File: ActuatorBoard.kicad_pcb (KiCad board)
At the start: 2 copper layers, 75 x 89.5 mm, 79 parts, among them J1 Screw_Terminal_01x02, J11 Screw_Terminal_01x02, J12 Screw_Terminal_01x02, J13 Screw_Terminal_01x04, J2 Screw_Terminal_01x02, J3 Screw_Terminal_01x02, J4 Screw_Terminal_01x02, J5 Screw_Terminal_01x02, J7 Screw_Terminal_01x02, J8 Screw_Terminal_01x02, J9 Screw_Terminal_01x02, K1 SANYOU_SRD_Form_B, K2 SANYOU_SRD_Form_B, K3 SANYOU_SRD_Form_B, P1 CONN_01X03, P10 CONN_01X03, P11 CONN_01X03, P12 CONN_01X03, P13 CONN_01X02, P14 SERVO_+, P15 SERVO_-, P16 CONN_01X03, P17 CONN_01X05, P18 CONN_01X08, P19 CONN_01X05, P2 CAN_Conn, P20 CONN_01X08, P21 STEPPER_VCC, P22 CONN_01X05, P23 CONN_01X04, P3 CONN_01X03, P4 CONN_01X03, P5 CONN_01X03, P7 CONN_01X03, P8 CONN_01X03, Q1 BS170, Q2 BS170, Q3 BS170, Q5 IRLR024, U1 MCP2551-I-SN, U2 AT90CAN128-16AU, U3 ULN2003, U4 L7805, Y1 Crystal, Y2 Crystal

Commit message: Added output files
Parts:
- added P6: CONN_01X06, Pin_Headers:Pin_Header_Straight_1x06, F.Cu at (181.4, 76.3)
- added REF**: 1pin, Connect:1pin, F.Cu at (199.1, 105.4)
- added REF**: 1pin, Connect:1pin, F.Cu at (202.3, 79.6)
- added REF**: 1pin, Connect:1pin, F.Cu at (220.3, 65.6)
- added REF**: 1pin, Connect:1pin, F.Cu at (208.5, 43.0)
- added REF**: 1pin, Connect:1pin, F.Cu at (176.1, 49.4)
- moved P20 22.5 mm to (167.1, 26.2), turned to 90 degrees
- moved P18 22.2 mm to (167.1, 28.8), turned to 90 degrees
- moved J3 20.9 mm to (233.2, 29.4), turned to 180 degrees
- moved D3 16.3 mm to (200.2, 43.6)
- moved R9 14.5 mm to (200.2, 41.7), turned to 0 degrees
- moved D7 11.6 mm to (227.9, 46.9), turned to 180 degrees
- moved R10 10.1 mm to (224.3, 46.9), turned to 0 degrees
- moved J2 9.71 mm to (222.5, 29.4), turned to 180 degrees
- moved C4 9.59 mm to (208.4, 36.7), turned to 0 degrees
- moved C2 9.00 mm to (209.6, 36.7), turned to 180 degrees
- moved D2 7.89 mm to (212.3, 28.5), turned to 90 degrees
- moved C3 5.47 mm to (219.7, 42.9), turned to 270 degrees
- moved D8 5.15 mm to (234.9, 97.2), turned to 180 degrees
- moved Q5 4.27 mm to (234.3, 41.4)
- moved D10 3.90 mm to (163.1, 94.2), turned to 0 degrees
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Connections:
- P22 pad 1: +5V -> PF2
- P22 pad 2: +5V -> PF2
- P22 pad 3: +5V -> PF2
- P22 pad 4: +5V -> PF2
- P22 pad 5: +5V -> PF2
- R11 pad 2: Net-(R11-Pad2) -> D2
- R12 pad 2: Net-(R12-Pad2) -> D1
- S1 pad 3: RX0 -> TX0
- S1 pad 4: TX0 -> RX0
- U2 pad 10: STEP -> DIRECTION
- U2 pad 11: DIRECTION -> STEP
- U2 pad 20: (no net) -> RESET
- U2 pad 44: Net-(R11-Pad2) -> MINI_M3
- U2 pad 45: Net-(R12-Pad2) -> MINI_M2
- U2 pad 46: MINI_M3 -> D2
- U2 pad 47: MINI_M2 -> D1
- U3 pad 1: R1 -> R2
- U3 pad 13: R2_SIG -> R1_SIG
- U3 pad 14: R2_SIG -> R1_SIG
- U3 pad 15: R1_SIG -> R2_SIG
- U3 pad 16: R1_SIG -> R2_SIG
- U3 pad 2: R1 -> R2
- U3 pad 3: R2 -> R1
- U3 pad 4: R2 -> R1
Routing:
- net PF2: track 0.00 -> 292.9 mm, vias 0 -> 2
- net +12V: track 0.00 -> 226.9 mm, vias 0 -> 4
- net +5V: track 0.00 -> 158.3 mm, vias 0 -> 5
- net GND: track 0.00 -> 121.1 mm, vias 0 -> 5
- net PC7: track 0.00 -> 58.2 mm, vias 0 -> 2
- net PC6: track 0.00 -> 52.8 mm, vias 0 -> 2
- net PC5: track 0.00 -> 49.8 mm, vias 0 -> 2
- net TX0: track 0.00 -> 43.9 mm, vias 0 -> 3
- net RX0: track 0.00 -> 41.6 mm, vias 0 -> 4
- net PC4: track 0.00 -> 41.4 mm
- net PC3: track 0.00 -> 38.7 mm
- net MINI_M3: track 0.00 -> 37.8 mm, vias 0 -> 2
- net PC2: track 0.00 -> 36.8 mm
- net STEP: track 0.00 -> 36.6 mm, vias 0 -> 1
- net PC1: track 0.00 -> 34.9 mm
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- added copper zone on B.Cu, net GND
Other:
- board text added: "3"
- board text added: "3A"
- board text added: "3B"
- board text added: "3C"
- board text added: "4"
- board text added: "5"
- board text added: "5VD"
- board text added: "6"
- board text added: "7"
- board text added: "AX-12"
- board text added: "F0"
- board text added: "F1"
- board text added: "GND"
- board text added: "H"
- board text added: "L"
- board text added: "ON=AX|OFF=PROG"
- board text added: "PB"
- board text added: "PC0"
- board text added: "PC1"
- board text added: "PC2"
- board text added: "PC3"
- board text added: "PC4"
- board text added: "PC5"
- board text added: "PC7"
- board text added: "RE"
- board text added: "RX"
- board text added: "SCK"
- board text added: "SCL"
- board text added: "SDA"
- board text added: "TX"
- board text added: "VCC"
- board text added: "http://elektropioneer.co.rs/ https://github.com/Elektropioneer Actuator Board V1"

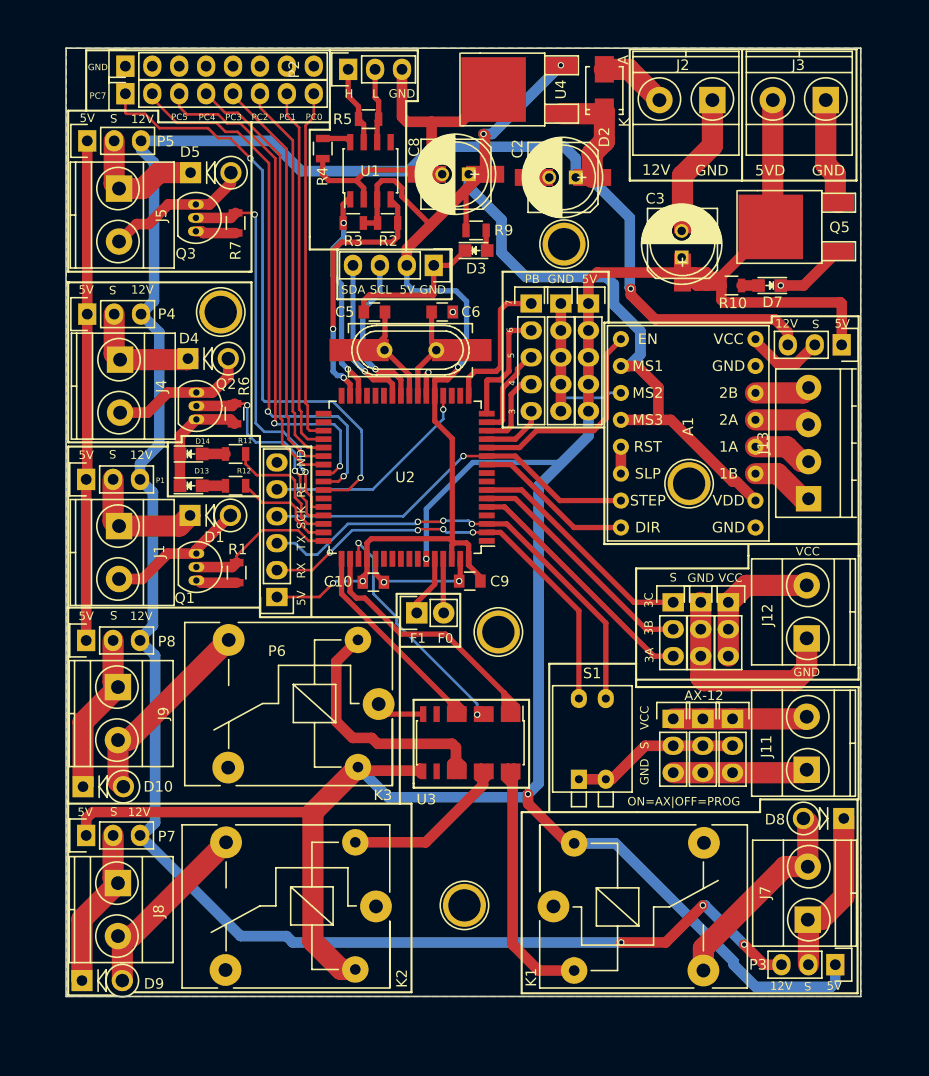
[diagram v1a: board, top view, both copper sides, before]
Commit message: Added new pdf, added tx rx debug pins
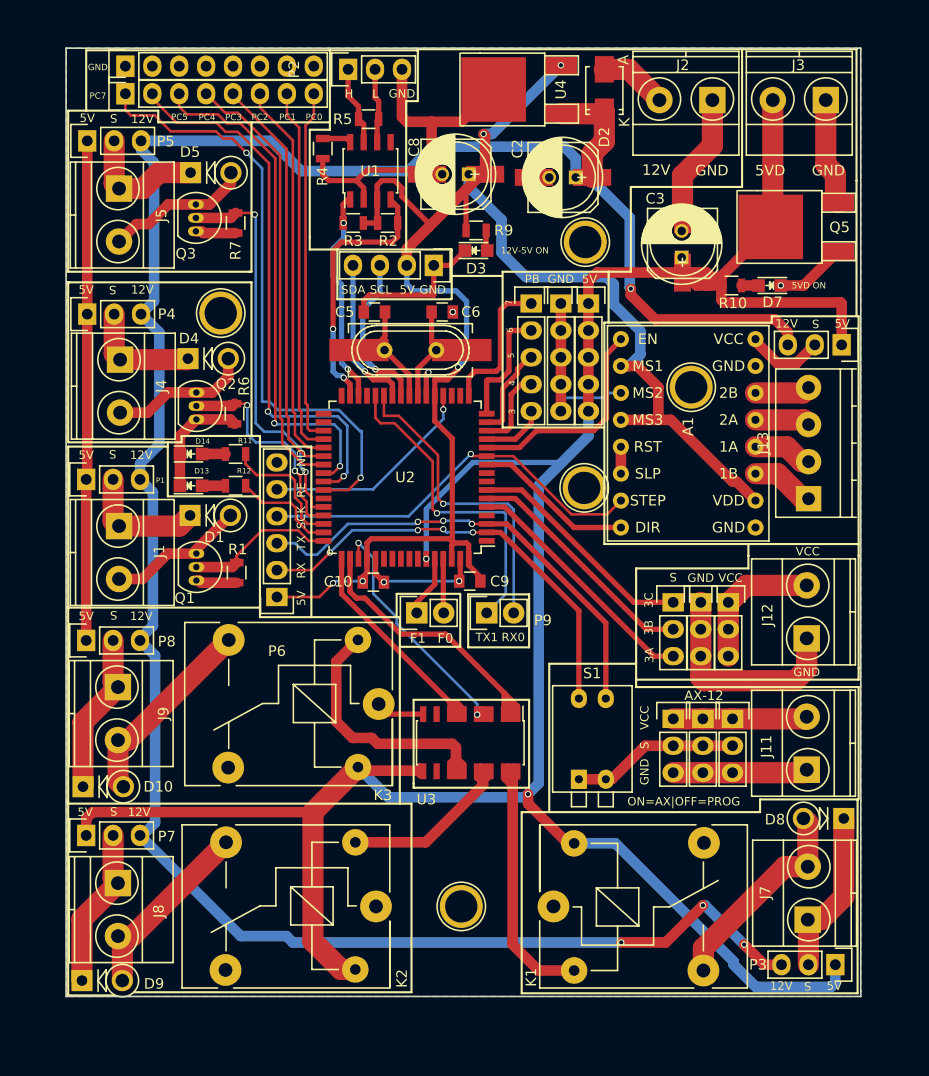
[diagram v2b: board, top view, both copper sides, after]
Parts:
- removed the REF** at (199.1, 105.4)
- removed the REF** at (202.3, 79.6)
- removed the REF** at (220.3, 65.6)
- removed the REF** at (208.5, 43.0)
- removed the REF** at (176.1, 49.4)
- added P9: CONN_01X02, Pin_Headers:Pin_Header_Straight_1x02, F.Cu at (201.2, 77.8)
- added REF**: 1pin, Connect:1pin, F.Cu at (176.1, 49.5)
- added REF**: 1pin, Connect:1pin, F.Cu at (210.5, 42.8)
- added REF**: 1pin, Connect:1pin, F.Cu at (220.5, 56.5)
- added REF**: 1pin, Connect:1pin, F.Cu at (198.8, 105.5)
- added REF**: 1pin, Connect:1pin, F.Cu at (210.4, 66.0)
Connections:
- U2 pad 27: (no net) -> RX1
- U2 pad 28: (no net) -> TX1
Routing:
- net TX1: track 0.00 -> 31.1 mm, vias 0 -> 1
- net RX1: track 0.00 -> 30.0 mm, vias 0 -> 1
- net STEP: track 36.6 -> 37.8 mm
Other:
- board text added: "12V-5V ON"
- board text added: "5VD ON"
- board text added: "RX0"
- board text added: "TX1"

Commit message: Added new wrl files, and did repairs
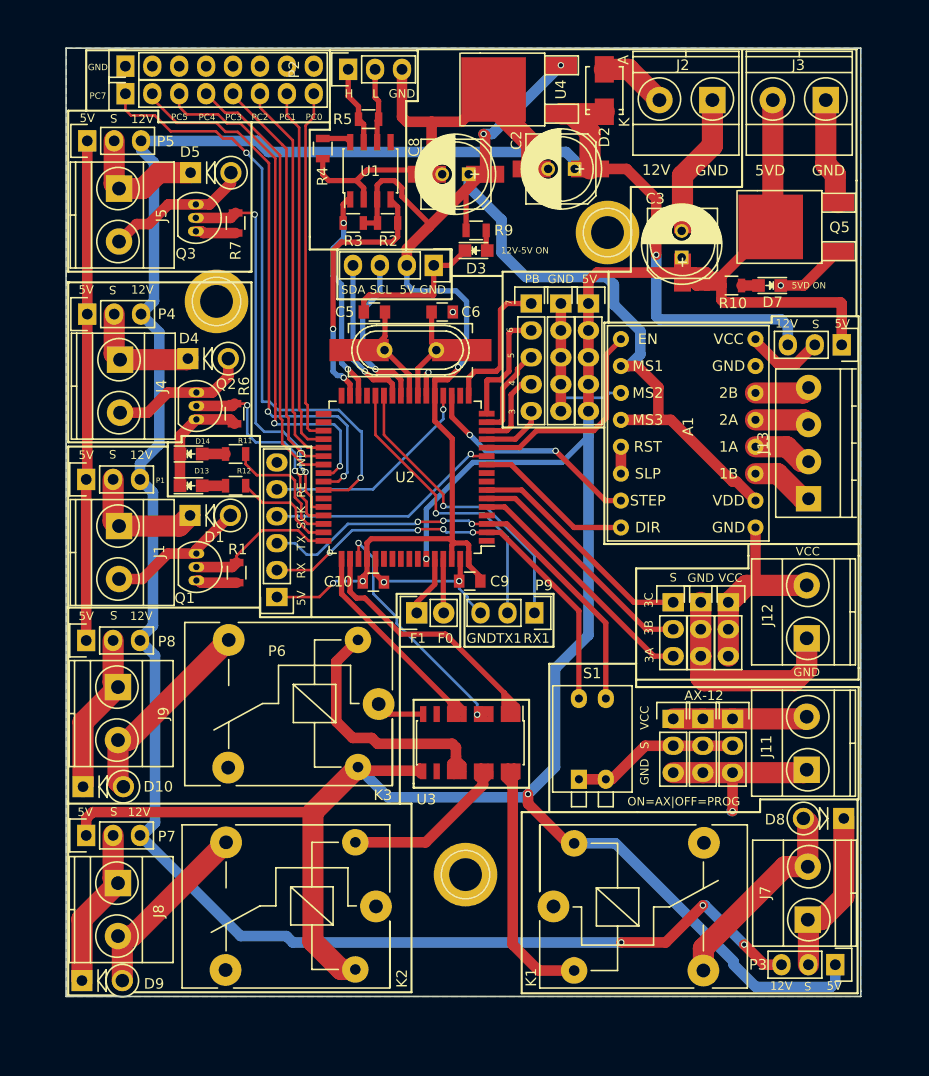
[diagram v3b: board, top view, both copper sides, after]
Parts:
- removed the REF** at (176.1, 49.5)
- removed the REF** at (210.5, 42.8)
- removed the REF** at (220.5, 56.5)
- removed the REF** at (198.8, 105.5)
- removed the REF** at (210.4, 66.0)
- added REF**: 1pin, Connect:1pin, F.Cu at (175.7, 48.4)
- added REF**: 1pin, Connect:1pin, F.Cu at (199.2, 102.5)
- added REF**: 1pin, Connect:1pin, F.Cu at (212.6, 41.9)
- C1, C2, C3, C4, C7, C8: value CP -> 100u
- C10, C9: value C -> 100n
- P9: value CONN_01X02 -> CONN_01X03; footprint Pin_Headers:Pin_Header_Straight_1x02 -> Pin_Headers:Pin_Header_Straight_1x03
- R10, R11, R12, R9: value 1K -> 330
- moved P9 4.50 mm to (205.7, 77.8), turned to 270 degrees
- moved C4 0.82 mm to (208.2, 35.9)
- moved C2 0.81 mm to (209.5, 35.9)
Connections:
- J11 pad 1: Net-(J11-Pad1) -> GND
- J12 pad 2: Net-(J12-Pad2) -> GND
- P10 pad 3: Net-(J11-Pad1) -> GND
- P11 pad 3: Net-(J11-Pad1) -> GND
- P12 pad 3: Net-(J11-Pad1) -> GND
- P15 pad 1: Net-(J12-Pad2) -> GND
- P15 pad 2: Net-(J12-Pad2) -> GND
- P15 pad 3: Net-(J12-Pad2) -> GND
- P6 pad 4: STEP -> SCK
- P9 pad 1: TX1 -> RX1
- P9 pad 2: RX1 -> TX1
- U2 pad 11: STEP -> SCK
- U2 pad 19: (no net) -> STEP
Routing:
- net GND: track 121.1 -> 169.2 mm, vias 5 -> 6
- net SCK: track 0.00 -> 22.3 mm, vias 0 -> 1
- net STEP: track 37.8 -> 21.2 mm, vias 1 -> 2
- net Net-(J12-Pad2): track 13.1 -> 0.00 mm
- net Net-(J11-Pad1): track 12.7 -> 0.00 mm
- net TX1: track 31.1 -> 28.4 mm
- net RX1: track 30.0 -> 28.7 mm
- net +12V: track 226.9 -> 225.9 mm
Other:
- board text added: "RX1"
- board text removed: "RX0"

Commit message: 12V relays...
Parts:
- removed REF** (x3): 1pin, Connect:1pin
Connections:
- K1 pad 5: PF2 -> +12V
- K2 pad 5: PF2 -> +12V
- K3 pad 5: PF2 -> +12V
- U3 pad 9: PF2 -> +12V
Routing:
- net +12V: track 225.9 -> 272.4 mm
- net GND: track 169.2 -> 206.1 mm, vias 6 -> 8
- net PF2: track 293.3 -> 306.0 mm, vias 2 -> 3

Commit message: 12V...
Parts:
- added REF**: 1pin, Connect:1pin, F.Cu at (175.7, 48.5)
- added REF**: 1pin, Connect:1pin, F.Cu at (199.1, 105.2)
- added REF**: 1pin, Connect:1pin, F.Cu at (212.6, 41.8)
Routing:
- net GND: track 206.1 -> 231.0 mm, vias 8 -> 12
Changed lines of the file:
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@@
     (area 161.424999 24.424999 236.575001 114.075001)
     (thickness 1.6)
-    (drawings 206)
-    (tracks 903)
+    (drawings 205)
+    (tracks 912)
     (zones 0)
-    (modules 81)
+    (modules 84)
     (nets 79)
   )
@@
     )
   )
-  (dimension 3.1 (width 0.3) (layer Dwgs.User)
-    (gr_text "3,100 mm" (at 155.35 48.35 270) (layer Dwgs.User)
-      (effects (font (size 1.5 1.5) (thickness 0.3)))
+  (module Connect:1pin (layer F.Cu)
+    (at 175.7 48.5)
+    (descr "module 1 pin (ou trou mecanique de percage)")
+    (tags DEV)
+    (fp_text reference REF** (at 0 -3.048) (layer F.SilkS) hide
+      (effects (font (size 1 1) (thickness 0.15)))
+    )
+    (fp_text value 1pin (at 0 2.794) (layer F.Fab) hide
+      (effects (font (size 1 1) (thickness 0.15)))
+    )
+    (fp_circle (center 0 0) (end 0 -2.286) (layer F.SilkS) (width 0.15))
+    (pad 1 thru_hole circle (at 0 0) (size 6 6) (drill 3.1) (layers *.Cu *.Mask F.SilkS))
+  )
+  (module Connect:1pin (layer F.Cu)
+    (at 199.1 105.2)
+    (descr "module 1 pin (ou trou mecanique de percage)")
+    (tags DEV)
+    (fp_text reference REF** (at 0 -3.048) (layer F.SilkS) hide
+      (effects (font (size 1 1) (thickness 0.15)))
+    )
+    (fp_text value 1pin (at 0 2.794) (layer F.Fab) hide
+      (effects (font (size 1 1) (thickness 0.15)))
+    )
+    (fp_circle (center 0 0) (end 0 -2.286) (layer F.SilkS) (width 0.15))
+    (pad 1 thru_hole circle (at 0 0) (size 6 6) (drill 3.1) (layers *.Cu *.Mask F.SilkS))
+  )
+  (module Connect:1pin (layer F.Cu)
+    (at 212.6 41.8)
+    (descr "module 1 pin (ou trou mecanique de percage)")
+    (tags DEV)
+    (fp_text reference REF** (at 0 -3.048) (layer F.SilkS) hide
+      (effects (font (size 1 1) (thickness 0.15)))
+    )
+    (fp_text value 1pin (at 0 2.794) (layer F.Fab) hide
+      (effects (font (size 1 1) (thickness 0.15)))
     )
-    (feature1 (pts (xy 175.7 49.95) (xy 156.8 49.95)))
-    (feature2 (pts (xy 175.7 46.85) (xy 156.8 46.85)))
-    (crossbar (pts (xy 159.5 46.85) (xy 159.5 49.95)))
-    (arrow1a (pts (xy 159.5 49.95) (xy 158.913579 48.823496)))
-    (arrow1b (pts (xy 159.5 49.95) (xy 160.086421 48.823496)))
-    (arrow2a (pts (xy 159.5 46.85) (xy 158.913579 47.976504)))
-    (arrow2b (pts (xy 159.5 46.85) (xy 160.086421 47.976504)))
+    (fp_circle (center 0 0) (end 0 -2.286) (layer F.SilkS) (width 0.15))
+    (pad 1 thru_hole circle (at 0 0) (size 6 6) (drill 3.1) (layers *.Cu *.Mask F.SilkS))
   )
   (gr_text RX1 (at 205.9 80.2) (layer F.SilkS)
@@
     (effects (font (size 0.8 0.8) (thickness 0.2)))
   )
-  (segment (start 211.85 89.65) (end 211.9 89.65) (width 1) (layer B.Cu) (net 1))
-  (via (at 204.65 83.85) (size 0.6) (drill 0.4) (layers F.Cu B.Cu) (net 1))
-  (segment (start 204.65 84.2) (end 204.65 83.85) (width 1) (layer F.Cu) (net 1))
-  (segment (start 209.25 88.8) (end 204.65 84.2) (width 1) (layer F.Cu) (net 1))
-  (segment (start 211.05 88.8) (end 209.25 88.8) (width 1) (layer F.Cu) (net 1))
-  (segment (start 211.9 89.65) (end 211.05 88.8) (width 1) (layer F.Cu) (net 1))
-  (via (at 211.9 89.65) (size 0.6) (drill 0.4) (layers F.Cu B.Cu) (net 1))
-  (segment (start 181.4 63.6) (end 181.4 63.25) (width 1) (layer F.Cu) (net 1) (status C00000))
-  (segment (start 181.4 63.25) (end 180.25 62.1) (width 1) (layer F.Cu) (net 1) (status 400000))
+  (via (at 220.1 53) (size 0.6) (drill 0.4) (layers F.Cu B.Cu) (net 1))
+  (via (at 221.6 48.1) (size 0.6) (drill 0.4) (layers F.Cu B.Cu) (net 1))
+  (segment (start 221.6 48.1) (end 221.6 51.5) (width 1) (layer F.Cu) (net 1))
+  (segment (start 221.6 51.5) (end 220.1 53) (width 1) (layer F.Cu) (net 1))
+  (segment (start 204.6 84.3) (end 204.7 84.3) (width 1) (layer B.Cu) (net 1))
+  (via (at 210.6 88.5) (size 0.6) (drill 0.4) (layers F.Cu B.Cu) (net 1))
+  (segment (start 208.9 88.5) (end 210.6 88.5) (width 1) (layer F.Cu) (net 1))
+  (segment (start 204.7 84.3) (end 208.9 88.5) (width 1) (layer F.Cu) (net 1))
+  (via (at 204.7 84.3) (size 0.6) (drill 0.4) (layers F.Cu B.Cu) (net 1))
+  (segment (start 207.5 105.5) (end 207.5 102.3) (width 1) (layer F.Cu) (net 1) (status 400000))
+  (via (at 205.2 95.1) (size 0.6) (drill 0.4) (layers F.Cu B.Cu) (net 1))
+  (segment (start 205.2 100) (end 205.2 95.1) (width 1) (layer F.Cu) (net 1))
+  (segment (start 207.5 102.3) (end 205.2 100) (width 1) (layer F.Cu) (net 1))
+  (segment (start 190.75 105.5) (end 191.9 105.5) (width 1) (layer F.Cu) (net 1) (status C00000))
+  (segment (start 191.9 105.5) (end 198.3 99.1) (width 1) (layer F.Cu) (net 1) (status 400000))
+  (via (at 198.3 99.1) (size 0.6) (drill 0.4) (layers F.Cu B.Cu) (net 1))
+  (segment (start 181.4 63.6) (end 181.4 63.25) (width 1) (layer F.Cu) (net 1))
+  (segment (start 181.4 63.25) (end 180.25 62.1) (width 1) (layer F.Cu) (net 1))
   (segment (start 180.25 62.1) (end 180.25 61.35) (width 1) (layer F.Cu) (net 1))
   (segment (start 180.25 61.35) (end 178.85 59.95) (width 1) (layer F.Cu) (net 1))
-  (segment (start 178.85 59.95) (end 177.4 59.95) (width 1) (layer F.Cu) (net 1) (status 800000))
+  (segment (start 178.85 59.95) (end 177.4 59.95) (width 1) (layer F.Cu) (net 1))
   (segment (start 177.5 41.95) (end 178.1 41.95) (width 0.25) (layer F.Cu) (net 1))
   (segment (start 178.1 41.95) (end 179.4 43.25) (width 0.25) (layer F.Cu) (net 1))
